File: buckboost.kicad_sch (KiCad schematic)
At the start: 25 parts, among them Q3 DUAL_N_FET, Q4 DUAL_N_FET, U4 LM5176

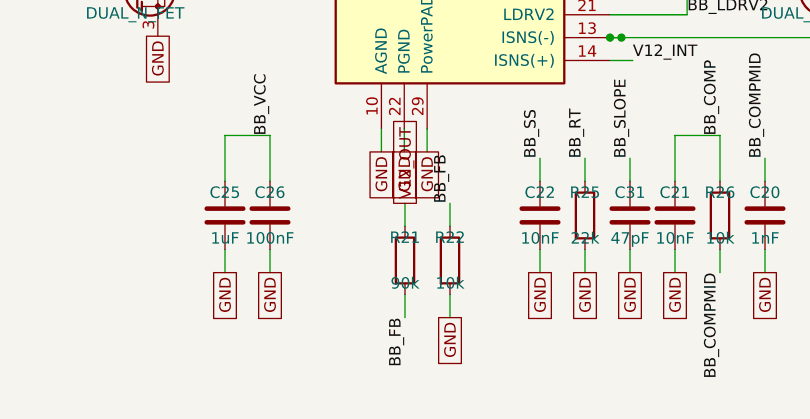
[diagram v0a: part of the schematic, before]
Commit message: schematic: parts pass + cell-holder and USB-C symbol swaps
- Apply Footprint + LCSC + Description to all 67 non-cell components
  across bms / charger / buckboost (JLCPCB-friendly BOM).
- Add project-local power_module_lib (symbols + footprints fetched via
  easyeda2kicad for BH-18650-B5BA016 holder and the two custom-package
  inductors).
- bms: replace BT1-3 (3x Battery_Cell) with single 6-pin BAT1 holder
  (BH-18650-B5BA016, C19184086). Pin mapping respects all-cells-same-
  direction; CELL1_TOP/CELL2_TOP taps repeat on inner pins.
- charger: swap J1 from USB_C_Receptacle_PowerOnly_24P to
  USB_C_Receptacle_USB2.0_16P (matches HRO TYPE-C-31-M-12 16P
  footprint). NC the 6 unused USB 2.0 data + SBU pins.
- R21 value 90k -> 91k (E96 standard so 0603 1% available at JLC).
- ERC on charger dropped 9 -> 2 (remaining: pre-existing Input Power
  flag, plus harmless 'fp-lib-table missing' warning resolved at
  project scope).

Co-Authored-By: Claude Opus 4.7 <noreply@anthropic.com>
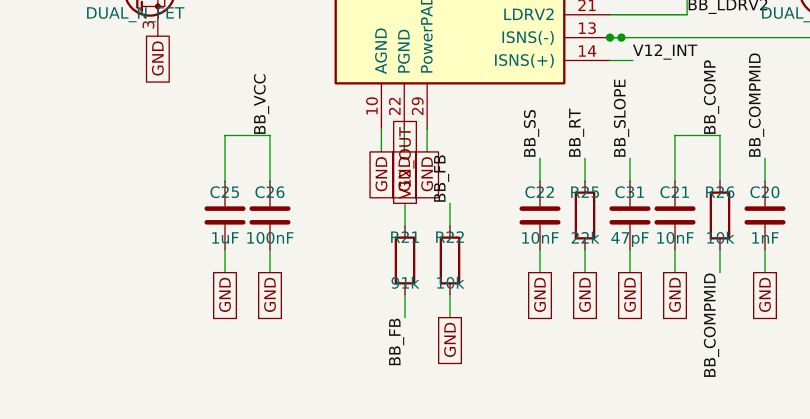
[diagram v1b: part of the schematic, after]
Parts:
- C20: footprint (none) -> Capacitor_SMD:C_0603_1608Metric; LCSC (none) -> C1588
- C21, C22: footprint (none) -> Capacitor_SMD:C_0603_1608Metric; LCSC (none) -> C57112
- C23, C24, C26, C28, C30: footprint (none) -> Capacitor_SMD:C_0603_1608Metric; LCSC (none) -> C14663
- C25: footprint (none) -> Capacitor_SMD:C_0805_2012Metric; LCSC (none) -> C28323
- C27: footprint (none) -> Capacitor_SMD:C_0805_2012Metric; LCSC (none) -> C15850
- C29: footprint (none) -> Capacitor_SMD:C_1206_3216Metric; LCSC (none) -> C12891
- C31: footprint (none) -> Capacitor_SMD:C_0603_1608Metric; LCSC (none) -> C1671
- D2: LCSC (none) -> C84259
- L2: footprint Inductor_SMD:L_12x12mm_H8mm -> power_module_lib:IND-SMD_L7.1-W6.6; LCSC (none) -> C41407100
- Q3, Q4: footprint (none) -> Package_SO:SOIC-8_3.9x4.9mm_P1.27mm; LCSC (none) -> C353066
- R20: footprint Resistor_SMD:R_2512_6332Metric -> Resistor_SMD:R_1206_3216Metric; LCSC (none) -> C2988648
- R21: value 90k -> 91k; footprint (none) -> Resistor_SMD:R_0603_1608Metric; LCSC (none) -> C2907077
- R22, R26: footprint (none) -> Resistor_SMD:R_0603_1608Metric; LCSC (none) -> C25804
- R23: footprint (none) -> Resistor_SMD:R_0603_1608Metric; LCSC (none) -> C25803
- R24: footprint (none) -> Resistor_SMD:R_0603_1608Metric; LCSC (none) -> C4184
- R25: footprint (none) -> Resistor_SMD:R_0603_1608Metric; LCSC (none) -> C31850
- R27: footprint (none) -> Resistor_SMD:R_0603_1608Metric; LCSC (none) -> C21190
- U4: footprint Package_SO:HTSSOP-28-1EP_4.4x9.7mm_P0.65mm_EP3.4x9.5mm_ThermalVias -> Package_SO:HTSSOP-28-1EP_4.4x9.7mm_P0.65mm_EP3.4x5.4mm; LCSC (none) -> C442493

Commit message: pcb: sync 71 footprints from schematic (full hierarchical import)
After the MCP-server restart picked up the hierarchical-sync fix,
re-syncing imported all 71 footprints (J2/J3/SW1 from the parent
sheet plus the 67 child-sheet components plus BAT1 and J1, then U4
manually after fixing its missing-footprint reference to the
EP2.85x5.4mm_ThermalVias HTSSOP-28 variant).  256 pads have nets
assigned.

Footprints are sitting in an off-board grid above y=0; placement
into the board area happens in the next step (#89 layout pass).

Also: add .gitignore for *_erc.json artifacts.

Co-Authored-By: Claude Opus 4.7 <noreply@anthropic.com>
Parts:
- U4: footprint Package_SO:HTSSOP-28-1EP_4.4x9.7mm_P0.65mm_EP3.4x5.4mm -> Package_SO:HTSSOP-28-1EP_4.4x9.7mm_P0.65mm_EP2.85x5.4mm_ThermalVias
